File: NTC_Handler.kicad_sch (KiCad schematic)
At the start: 48 parts, among them U11 LMV7239M5/NOPB, U2 LM1117GS-5.0, U3 LM1117GS-5.0, U4 LMV7239M5/NOPB, U5 ADuM1200AR, U6 ADuM1200AR, U7 LM1117GS-5.0, U8 LMV7239M5/NOPB, U9 ADuM1200AR

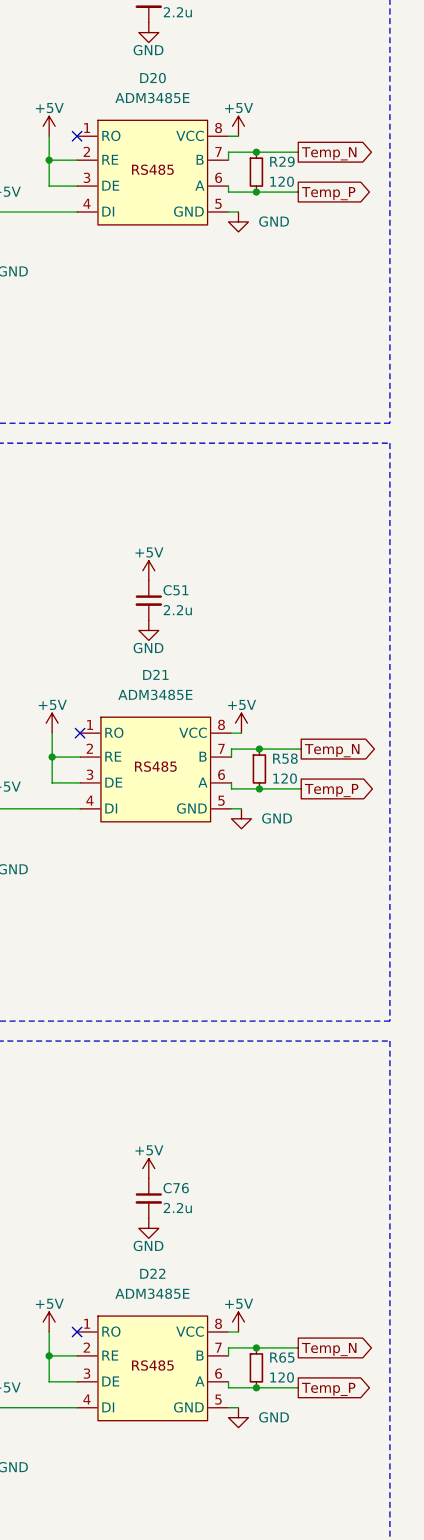
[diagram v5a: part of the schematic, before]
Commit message: Добавил новые разъёмы
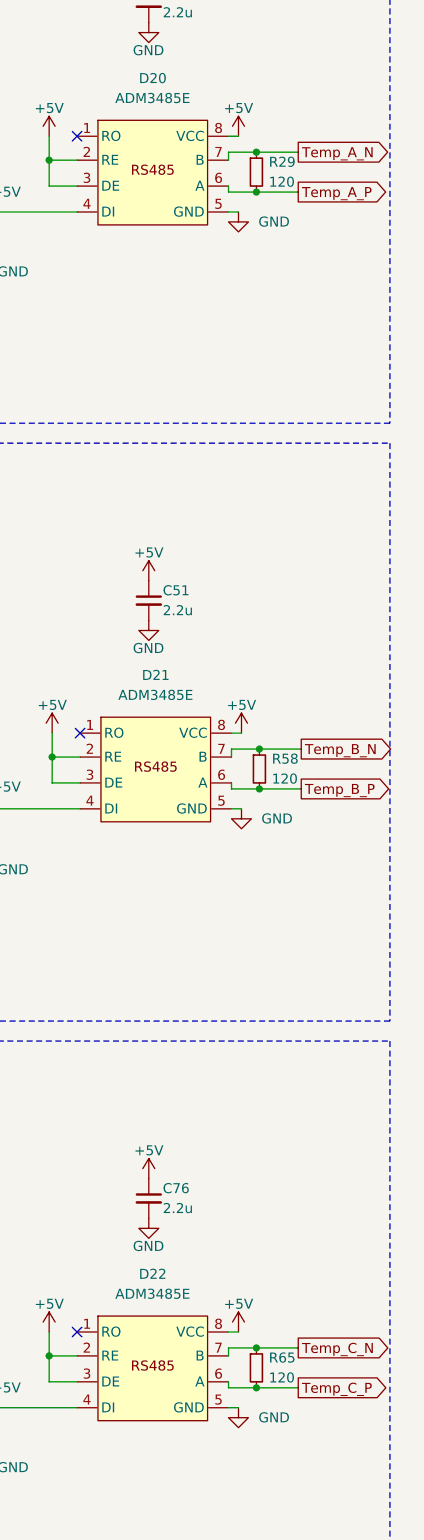
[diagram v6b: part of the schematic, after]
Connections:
- removed net Temp_N: D20.7 (B), D21.7 (B), D22.7 (B), R29.1, R58.1, R65.1
- removed net Temp_P: D20.6 (A), D21.6 (A), D22.6 (A), R29.2, R58.2, R65.2
- new net Temp_A_N: D20.7 (B), R29.1
- new net Temp_A_P: D20.6 (A), R29.2
- new net Temp_B_N: D21.7 (B), R58.1
- new net Temp_B_P: D21.6 (A), R58.2
- new net Temp_C_N: D22.7 (B), R65.1
- new net Temp_C_P: D22.6 (A), R65.2
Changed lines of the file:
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@@
 		)
 	)
-	(global_label "Temp_P"
+	(global_label "Temp_B_P"
 		(shape output)
 		(at 270.002 147.574 0)
@@
 		)
 		(property "Intersheetrefs" "${INTERSHEET_REFS}"
-			(at 279.5513 147.4946 0)
+			(at 282.3609 147.574 0)
 			(effects
 				(font
@@
 		)
 	)
-	(global_label "Temp_P"
+	(global_label "Temp_C_P"
 		(shape output)
 		(at 269.621 223.901 0)
@@
 		)
 		(property "Intersheetrefs" "${INTERSHEET_REFS}"
-			(at 279.1703 223.8216 0)
+			(at 281.9799 223.901 0)
 			(effects
 				(font
@@
 		)
 	)
-	(global_label "Temp_N"
+	(global_label "Temp_C_N"
 		(shape output)
 		(at 269.621 218.821 0)
@@
 		)
 		(property "Intersheetrefs" "${INTERSHEET_REFS}"
-			(at 279.2308 218.7416 0)
+			(at 282.0404 218.821 0)
 			(effects
 				(font
@@
 		)
 	)
-	(global_label "Temp_N"
+	(global_label "Temp_B_N"
 		(shape output)
 		(at 270.002 142.494 0)
@@
 		)
 		(property "Intersheetrefs" "${INTERSHEET_REFS}"
-			(at 279.6118 142.4146 0)
+			(at 282.4214 142.494 0)
 			(effects
 				(font
@@
 		)
 	)
-	(global_label "Temp_P"
+	(global_label "Temp_A_P"
 		(shape output)
 		(at 269.621 71.501 0)
@@
 		)
 		(property "Intersheetrefs" "${INTERSHEET_REFS}"
-			(at 279.1703 71.4216 0)
-			(effects
-				(font
-					(size 1.27 1.27)
-				)
-				(justify left)
-				(hide yes)
-			)
-		)
-	)
-	(global_label "Temp_N"
+			(at 281.7985 71.501 0)
+			(effects
+				(font
+					(size 1.27 1.27)
+				)
+				(justify left)
+				(hide yes)
+			)
+		)
+	)
+	(global_label "Temp_A_N"
 		(shape output)
 		(at 269.621 66.421 0)
@@
 		)
 		(property "Intersheetrefs" "${INTERSHEET_REFS}"
-			(at 279.2308 66.3416 0)
-			(effects
-				(font
+			(at 281.859 66.421 0)
+			(effects
+				(font

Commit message: Развел вторую стойку
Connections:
- net Temp_C_N is gone; now on net Temp_A_N: D22.7 (B), R65.1
- net Temp_C_P is gone; now on net Temp_A_P: D22.6 (A), R65.2
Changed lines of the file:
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@@
 		)
 	)
-	(global_label "Temp_C_P"
+	(global_label "Temp_A_P"
 		(shape output)
 		(at 269.621 223.901 0)
@@
 		)
 		(property "Intersheetrefs" "${INTERSHEET_REFS}"
-			(at 281.9799 223.901 0)
+			(at 281.7985 223.901 0)
 			(effects
 				(font
@@
 		)
 	)
-	(global_label "Temp_C_N"
+	(global_label "Temp_A_N"
 		(shape output)
 		(at 269.621 218.821 0)
@@
 		)
 		(property "Intersheetrefs" "${INTERSHEET_REFS}"
-			(at 282.0404 218.821 0)
+			(at 281.859 218.821 0)
 			(effects
 				(font

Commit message: Развел все
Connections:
- net Temp_A_N: no longer D20.7 (B), R29.1
- net Temp_A_P: no longer D20.6 (A), R29.2
- removed net GNDPWR: C27.2, C28.2, C29.2, C40.2, C50.2, C52.2, C55.2, C56.2, C75.2, C77.2, C80.2, C81.2, R26.1, R59.1, R70.1, U11.2 (V-), U2.1 (GND), U3.1 (GND), U4.2 (V-), U5.4 (GND1), U6.4 (GND1), U7.1 (GND), U8.2 (V-), U9.4 (GND1)
- new net -15V_L1: C75.2, C77.2, C80.2, C81.2, R70.1, U7.1 (GND), U8.2 (V-), U9.4 (GND1)
- new net -15V_L2: C50.2, C52.2, C55.2, C56.2, R59.1, U3.1 (GND), U4.2 (V-), U6.4 (GND1)
- new net -15V_L3: C27.2, C28.2, C29.2, C40.2, R26.1, U11.2 (V-), U2.1 (GND), U5.4 (GND1)
- new net Temp_C_N: D20.7 (B), R29.1
- new net Temp_C_P: D20.6 (A), R29.2
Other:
- moved on the sheet: C40
